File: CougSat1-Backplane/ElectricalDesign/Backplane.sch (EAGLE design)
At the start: 17 parts, among them J1 CougSat Socket, J10 Separation Switch, J2 CougSat Socket, J3 CougSat Socket, J4 CougSat Socket, J5 CougSat Socket, J6 CougSat Socket, J7 CougSat Socket, J8 CougSat Socket, J9 Separation Switch

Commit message: Generate Gerbers
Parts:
- J10, J9: value Separation Switch -> CougSat Socket; device CougsInSpace-Connectors:1X04-PICOLOCK -> CougsInSpace-Connectors:CIS_CARD-SODIMM-DDR1
- J5, J6: value CougSat Socket -> Separation Switch; device CougsInSpace-Connectors:CIS_CARD-SODIMM-DDR1 -> CougsInSpace-Connectors:1X04-PICOLOCK
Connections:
- net BUS_I2C0_IRQ: now also J10DATA.BUS_I2C0_IRQ, J9DATA.BUS_I2C0_IRQ; no longer J5DATA.BUS_I2C0_IRQ, J6DATA.BUS_I2C0_IRQ
- net BUS_I2C0_SCL: now also J10DATA.BUS_I2C0_SCL, J9DATA.BUS_I2C0_SCL; no longer J5DATA.BUS_I2C0_SCL, J6DATA.BUS_I2C0_SCL
- net BUS_I2C0_SDA: now also J10DATA.BUS_I2C0_SDA, J9DATA.BUS_I2C0_SDA; no longer J5DATA.BUS_I2C0_SDA, J6DATA.BUS_I2C0_SDA
- net BUS_I2C1_IRQ: now also J10DATA.BUS_I2C1_IRQ, J9DATA.BUS_I2C1_IRQ; no longer J5DATA.BUS_I2C1_IRQ, J6DATA.BUS_I2C1_IRQ
- net BUS_I2C1_SCL: now also J10DATA.BUS_I2C1_SCL, J9DATA.BUS_I2C1_SCL; no longer J5DATA.BUS_I2C1_SCL, J6DATA.BUS_I2C1_SCL
- net BUS_I2C1_SDA: now also J10DATA.BUS_I2C1_SDA, J9DATA.BUS_I2C1_SDA; no longer J5DATA.BUS_I2C1_SDA, J6DATA.BUS_I2C1_SDA
- net BUS_JTAG_EN-0: now also J10JTAG.BUS_JTAG_EN-0, J9JTAG.BUS_JTAG_EN-0; no longer J5JTAG.BUS_JTAG_EN-0, J6JTAG.BUS_JTAG_EN-0
- net BUS_JTAG_EN-1: now also J10JTAG.BUS_JTAG_EN-1, J9JTAG.BUS_JTAG_EN-1; no longer J5JTAG.BUS_JTAG_EN-1, J6JTAG.BUS_JTAG_EN-1
- net BUS_JTAG_EN-2: now also J10JTAG.BUS_JTAG_EN-2, J9JTAG.BUS_JTAG_EN-2; no longer J5JTAG.BUS_JTAG_EN-2, J6JTAG.BUS_JTAG_EN-2
- net BUS_JTAG_EN-3: now also J10JTAG.BUS_JTAG_EN-3, J9JTAG.BUS_JTAG_EN-3; no longer J5JTAG.BUS_JTAG_EN-3, J6JTAG.BUS_JTAG_EN-3
- net BUS_JTAG_TCK: now also J10JTAG.BUS_JTAG_TCK, J9JTAG.BUS_JTAG_TCK; no longer J5JTAG.BUS_JTAG_TCK, J6JTAG.BUS_JTAG_TCK
- net BUS_JTAG_TDI: now also J10JTAG.BUS_JTAG_TDI, J9JTAG.BUS_JTAG_TDI; no longer J5JTAG.BUS_JTAG_TDI, J6JTAG.BUS_JTAG_TDI
- net BUS_JTAG_TDO: now also J10JTAG.BUS_JTAG_TDO, J9JTAG.BUS_JTAG_TDO; no longer J5JTAG.BUS_JTAG_TDO, J6JTAG.BUS_JTAG_TDO
- net BUS_JTAG_TMS: now also J10JTAG.BUS_JTAG_TMS, J9JTAG.BUS_JTAG_TMS; no longer J5JTAG.BUS_JTAG_TMS, J6JTAG.BUS_JTAG_TMS
- net BUS_SPI_MISO: now also J10DATA.BUS_SPI_MISO, J9DATA.BUS_SPI_MISO; no longer J5DATA.BUS_SPI_MISO, J6DATA.BUS_SPI_MISO
- net BUS_SPI_MOSI: now also J10DATA.BUS_SPI_MOSI, J9DATA.BUS_SPI_MOSI; no longer J5DATA.BUS_SPI_MOSI, J6DATA.BUS_SPI_MOSI
- net BUS_SPI_SCK: now also J10DATA.BUS_SPI_SCK, J9DATA.BUS_SPI_SCK; no longer J5DATA.BUS_SPI_SCK, J6DATA.BUS_SPI_SCK
- net COM_SPI_CS: now also J10DATA.COM_SPI_CS, J9DATA.COM_SPI_CS; no longer J5DATA.COM_SPI_CS, J6DATA.COM_SPI_CS
- net COM_SPI_MISO: now also J10DATA.COM_SPI_MISO, J9DATA.COM_SPI_MISO; no longer J5DATA.COM_SPI_MISO, J6DATA.COM_SPI_MISO
- net COM_SPI_MOSI: now also J10DATA.COM_SPI_MOSI, J9DATA.COM_SPI_MOSI; no longer J5DATA.COM_SPI_MOSI, J6DATA.COM_SPI_MOSI
- net COM_SPI_SCK: now also J10DATA.COM_SPI_SCK, J9DATA.COM_SPI_SCK; no longer J5DATA.COM_SPI_SCK, J6DATA.COM_SPI_SCK
- net CTRL_!RESET: now also J10DATA.CTRL_!RESET, J9DATA.CTRL_!RESET; no longer J5DATA.CTRL_!RESET, J6DATA.CTRL_!RESET
- net CTRL_SYNC: now also J10DATA.CTRL_SYNC, J9DATA.CTRL_SYNC; no longer J5DATA.CTRL_SYNC, J6DATA.CTRL_SYNC
- net GPIO-0: now also J10GPIO.GPIO-0, J9GPIO.GPIO-0; no longer J5GPIO.GPIO-0, J6GPIO.GPIO-0
- net GPIO-1: now also J10GPIO.GPIO-1, J9GPIO.GPIO-1; no longer J5GPIO.GPIO-1, J6GPIO.GPIO-1
- net GPIO-2: now also J10GPIO.GPIO-2, J9GPIO.GPIO-2; no longer J5GPIO.GPIO-2, J6GPIO.GPIO-2
- net GPIO-3: now also J10GPIO.GPIO-3, J9GPIO.GPIO-3; no longer J5GPIO.GPIO-3, J6GPIO.GPIO-3
- net GPIO-4: now also J10GPIO.GPIO-4, J9GPIO.GPIO-4; no longer J5GPIO.GPIO-4, J6GPIO.GPIO-4
- net GPIO-5: now also J10GPIO.GPIO-5, J9GPIO.GPIO-5; no longer J5GPIO.GPIO-5, J6GPIO.GPIO-5
- net GPIO-6: now also J10GPIO.GPIO-6, J9GPIO.GPIO-6; no longer J5GPIO.GPIO-6, J6GPIO.GPIO-6
- net GPIO-7: now also J10GPIO.GPIO-7, J9GPIO.GPIO-7; no longer J5GPIO.GPIO-7, J6GPIO.GPIO-7
- net GPIO-8: now also J10GPIO.GPIO-8, J9GPIO.GPIO-8; no longer J5GPIO.GPIO-8, J6GPIO.GPIO-8
- net GPIO-9: now also J10GPIO.GPIO-9, J9GPIO.GPIO-9; no longer J5GPIO.GPIO-9, J6GPIO.GPIO-9
- net PGND: now also J10POWER.PGND, J5.3, J5.4, J6.3, J6.4, J9POWER.PGND; no longer J10.3, J10.4, J5POWER.PGND, J6POWER.PGND, J9.3, J9.4
- net PR_3.3V-0: now also J10POWER.PR_3.3V-0, J9POWER.PR_3.3V-0; no longer J5POWER.PR_3.3V-0, J6POWER.PR_3.3V-0
- net PR_3.3V-1: now also J10POWER.PR_3.3V-1, J9POWER.PR_3.3V-1; no longer J5POWER.PR_3.3V-1, J6POWER.PR_3.3V-1
- net PR_3.3V-10: now also J10POWER.PR_3.3V-10, J9POWER.PR_3.3V-10; no longer J5POWER.PR_3.3V-10, J6POWER.PR_3.3V-10
- net PR_3.3V-11: now also J10POWER.PR_3.3V-11, J9POWER.PR_3.3V-11; no longer J5POWER.PR_3.3V-11, J6POWER.PR_3.3V-11
- net PR_3.3V-12: now also J10POWER.PR_3.3V-12, J9POWER.PR_3.3V-12; no longer J5POWER.PR_3.3V-12, J6POWER.PR_3.3V-12
- net PR_3.3V-2: now also J10POWER.PR_3.3V-2, J9POWER.PR_3.3V-2; no longer J5POWER.PR_3.3V-2, J6POWER.PR_3.3V-2
- net PR_3.3V-3: now also J10POWER.PR_3.3V-3, J9POWER.PR_3.3V-3; no longer J5POWER.PR_3.3V-3, J6POWER.PR_3.3V-3
- net PR_3.3V-4: now also J10POWER.PR_3.3V-4, J9POWER.PR_3.3V-4; no longer J5POWER.PR_3.3V-4, J6POWER.PR_3.3V-4
- net PR_3.3V-5: now also J10POWER.PR_3.3V-5, J9POWER.PR_3.3V-5; no longer J5POWER.PR_3.3V-5, J6POWER.PR_3.3V-5
- net PR_3.3V-6: now also J10POWER.PR_3.3V-6, J9POWER.PR_3.3V-6; no longer J5POWER.PR_3.3V-6, J6POWER.PR_3.3V-6
- net PR_3.3V-7: now also J10POWER.PR_3.3V-7, J9POWER.PR_3.3V-7; no longer J5POWER.PR_3.3V-7, J6POWER.PR_3.3V-7
- net PR_3.3V-8: now also J10POWER.PR_3.3V-8, J9POWER.PR_3.3V-8; no longer J5POWER.PR_3.3V-8, J6POWER.PR_3.3V-8
- net PR_3.3V-9: now also J10POWER.PR_3.3V-9, J9POWER.PR_3.3V-9; no longer J5POWER.PR_3.3V-9, J6POWER.PR_3.3V-9
- net PR_BATT-0: now also J10POWER.PR_BATT-0, J9POWER.PR_BATT-0; no longer J5POWER.PR_BATT-0, J6POWER.PR_BATT-0
- net PR_BATT-1: now also J10POWER.PR_BATT-1, J9POWER.PR_BATT-1; no longer J5POWER.PR_BATT-1, J6POWER.PR_BATT-1
- net PR_BATT-2: now also J10POWER.PR_BATT-2, J9POWER.PR_BATT-2; no longer J5POWER.PR_BATT-2, J6POWER.PR_BATT-2
- net PR_BATT-3: now also J10POWER.PR_BATT-3, J9POWER.PR_BATT-3; no longer J5POWER.PR_BATT-3, J6POWER.PR_BATT-3
- net PR_BATT-4: now also J10POWER.PR_BATT-4, J9POWER.PR_BATT-4; no longer J5POWER.PR_BATT-4, J6POWER.PR_BATT-4
- net PR_BATT-5: now also J10POWER.PR_BATT-5, J9POWER.PR_BATT-5; no longer J5POWER.PR_BATT-5, J6POWER.PR_BATT-5
- net PR_BATT-6: now also J10POWER.PR_BATT-6, J9POWER.PR_BATT-6; no longer J5POWER.PR_BATT-6, J6POWER.PR_BATT-6
- net PWR_CTRL_SW: now also J10POWER.PWR_CTRL_SW, J5.1, J5.2, J6.1, J6.2, J9POWER.PWR_CTRL_SW; no longer J10.1, J10.2, J5POWER.PWR_CTRL_SW, J6POWER.PWR_CTRL_SW, J9.1, J9.2
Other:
- moved on the sheet: J7DATA, J7GPIO, J7JTAG, J7POWER, J8DATA, J8GPIO, J8JTAG, J8POWER, R1, R2

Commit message: Merge branch 'master' into panel+X
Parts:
- added LOGO100, LOGO3: Satellite 16mm, CougsInSpace-Aesthetics:CIS-LOGO-SATELLITE-16MM
- added LOGO2: SIGNATUREHENDRIK, CougsInSpace-Aesthetics:SIGNATUREHENDRIK
- J1, J10, J2, J3, J4, J7, J8, J9: device CougsInSpace-Connectors:CIS_CARD-SODIMM-DDR1 -> CougsInSpace-Connectors:CIS_CARD-PCIE
- LOGO1: value SIGNATUREBRADLEY -> Text; device CougsInSpace-Aesthetics:SIGNATUREBRADLEY -> CougsInSpace-Aesthetics:CIS-LOGO-TEXT
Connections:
- removed net CHASSIS: C1.1, C2.1, H1.MOUNT, H2.MOUNT, R1.2, R2.2
- removed net GPIO-6: J10GPIO.GPIO-6, J1GPIO.GPIO-6, J2GPIO.GPIO-6, J3GPIO.GPIO-6, J4GPIO.GPIO-6, J7GPIO.GPIO-6, J8GPIO.GPIO-6, J9GPIO.GPIO-6
- removed net GPIO-7: J10GPIO.GPIO-7, J1GPIO.GPIO-7, J2GPIO.GPIO-7, J3GPIO.GPIO-7, J4GPIO.GPIO-7, J7GPIO.GPIO-7, J8GPIO.GPIO-7, J9GPIO.GPIO-7
- removed net GPIO-8: J10GPIO.GPIO-8, J1GPIO.GPIO-8, J2GPIO.GPIO-8, J3GPIO.GPIO-8, J4GPIO.GPIO-8, J7GPIO.GPIO-8, J8GPIO.GPIO-8, J9GPIO.GPIO-8
- removed net GPIO-9: J10GPIO.GPIO-9, J1GPIO.GPIO-9, J2GPIO.GPIO-9, J3GPIO.GPIO-9, J4GPIO.GPIO-9, J7GPIO.GPIO-9, J8GPIO.GPIO-9, J9GPIO.GPIO-9
- new net CHASSIS1: C1.1, H1.MOUNT, R1.2
- new net CHASSIS2: C2.1, H2.MOUNT, R2.2
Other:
- moved on the sheet: C1, C2, H1, H2, J10JTAG, J1JTAG, J2JTAG, J3JTAG, J4JTAG, J7JTAG, J8JTAG, J9JTAG

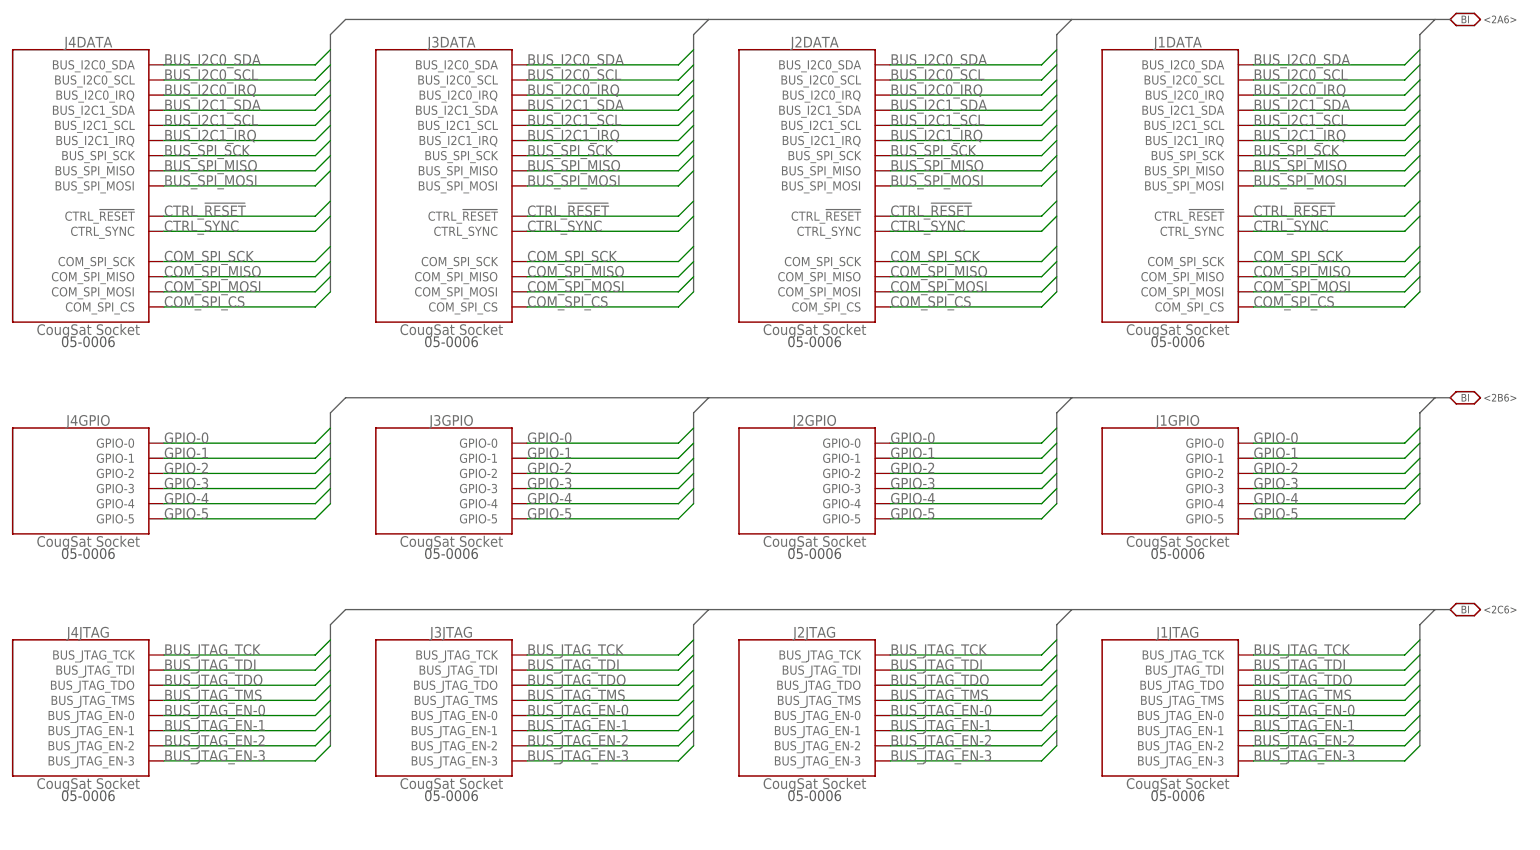
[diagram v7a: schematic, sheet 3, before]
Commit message: Switched CTRL_RESET to GPIO pins
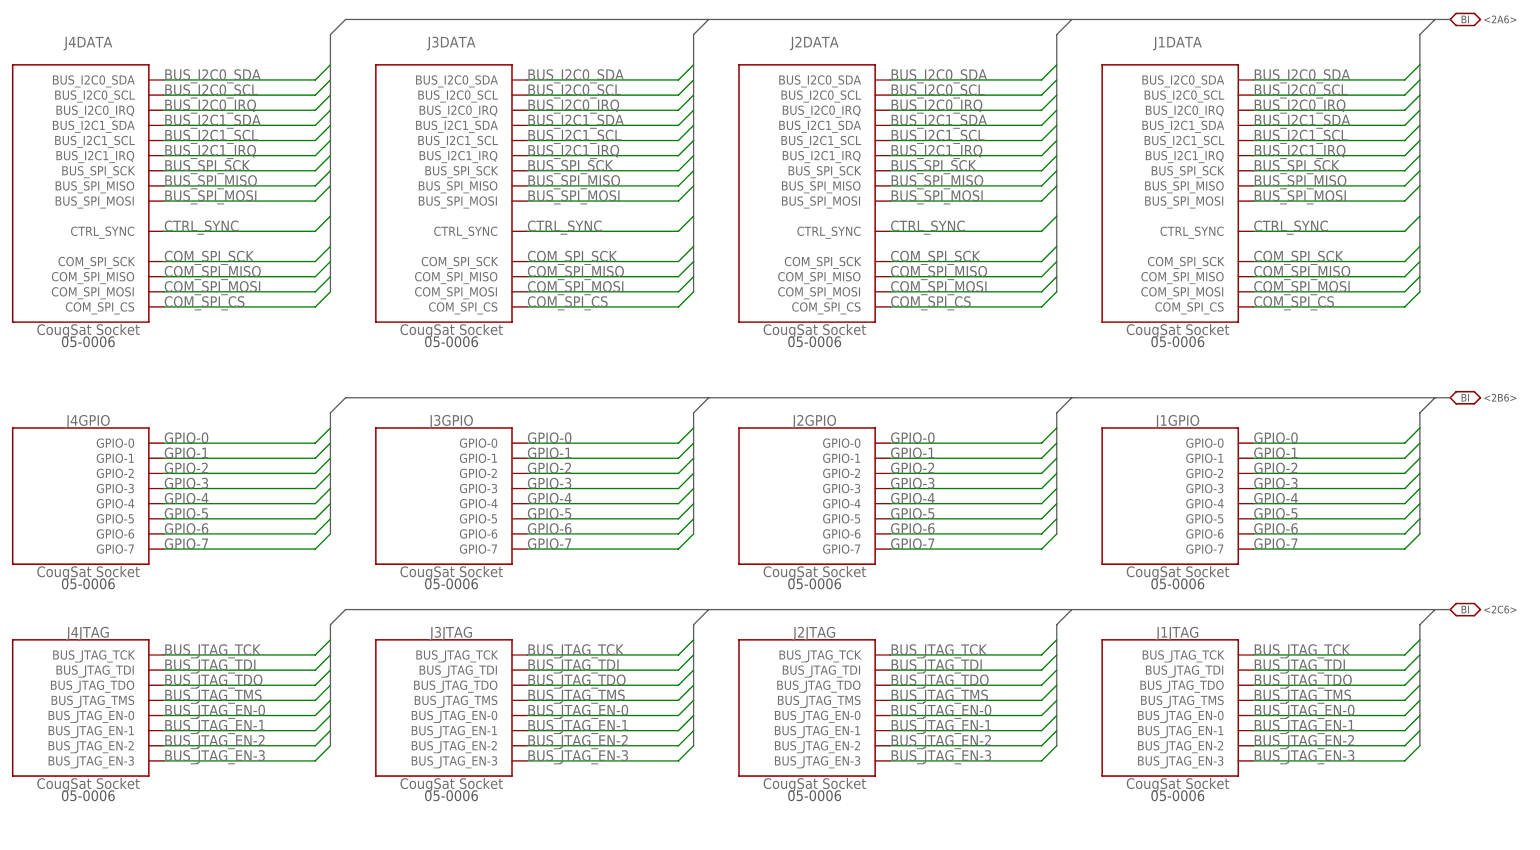
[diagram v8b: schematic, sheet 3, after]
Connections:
- removed net CTRL_!RESET: J10DATA.CTRL_!RESET, J1DATA.CTRL_!RESET, J2DATA.CTRL_!RESET, J3DATA.CTRL_!RESET, J4DATA.CTRL_!RESET, J7DATA.CTRL_!RESET, J8DATA.CTRL_!RESET, J9DATA.CTRL_!RESET
- new net GPIO-6: J10GPIO.GPIO-6, J1GPIO.GPIO-6, J2GPIO.GPIO-6, J3GPIO.GPIO-6, J4GPIO.GPIO-6, J7GPIO.GPIO-6, J8GPIO.GPIO-6, J9GPIO.GPIO-6
- new net GPIO-7: J10GPIO.GPIO-7, J1GPIO.GPIO-7, J2GPIO.GPIO-7, J3GPIO.GPIO-7, J4GPIO.GPIO-7, J7GPIO.GPIO-7, J8GPIO.GPIO-7, J9GPIO.GPIO-7
